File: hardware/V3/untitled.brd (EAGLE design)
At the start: 74 x 61.8 mm, 27 parts, among them U1 ADAFRUIT_MPL3115A2_BAROMETER, U2 ADAFRUIT_MTK3339_GPS, U4 SPARKFUN_MPU9250_IMU, U5 RFM95W-915S2

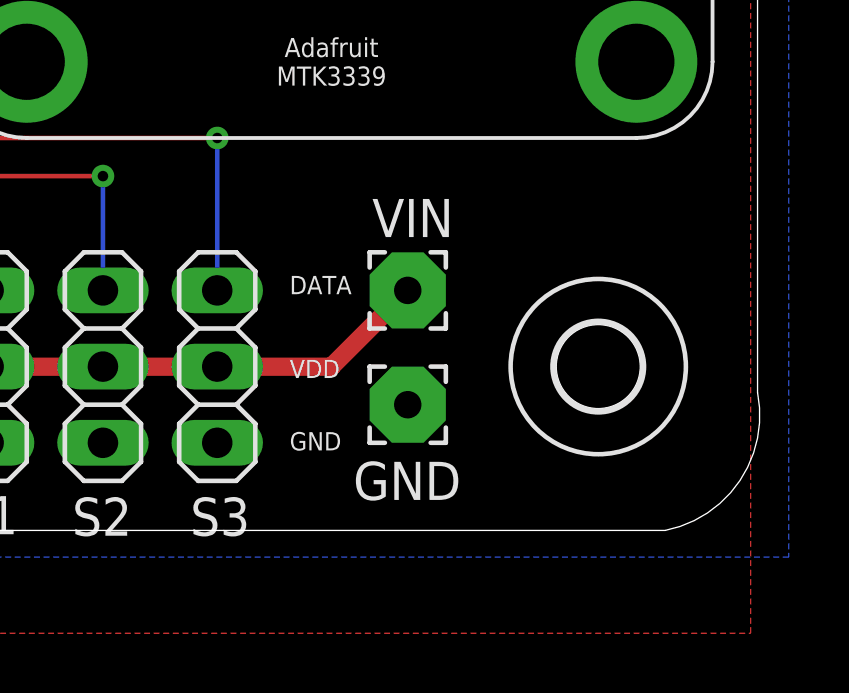
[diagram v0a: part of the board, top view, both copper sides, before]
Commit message: added screw terminal to board; combined filter with imu scope
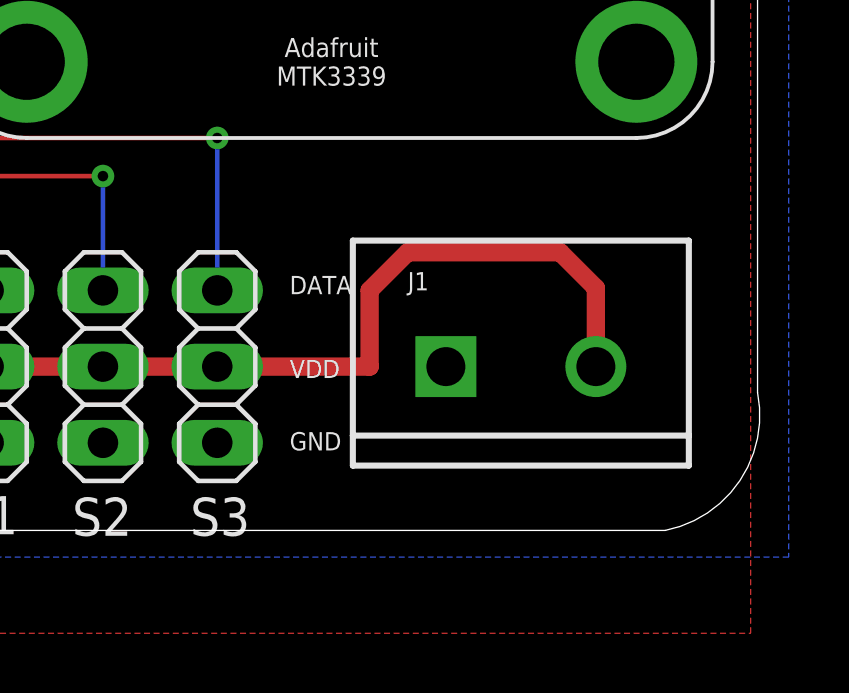
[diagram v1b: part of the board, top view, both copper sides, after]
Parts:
- removed GND, VIN: (no value), wirepad:2,54/0,9
- removed H2: MOUNT-HOLE2.8, holes:2,8
- added J1: (no value), SparkFun-Connectors:SCREWTERMINAL-5MM-2
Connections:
- net GND: now also J1.1; no longer GND.1
- net VIN: now also J1.2; no longer VIN.1
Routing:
- net VIN: track 42.0 -> 53.4 mm
